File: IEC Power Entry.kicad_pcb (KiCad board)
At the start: 2 copper layers, 66 x 70.3 mm, 13 parts, among them J1 Primary, P3 DD21.0121.1111

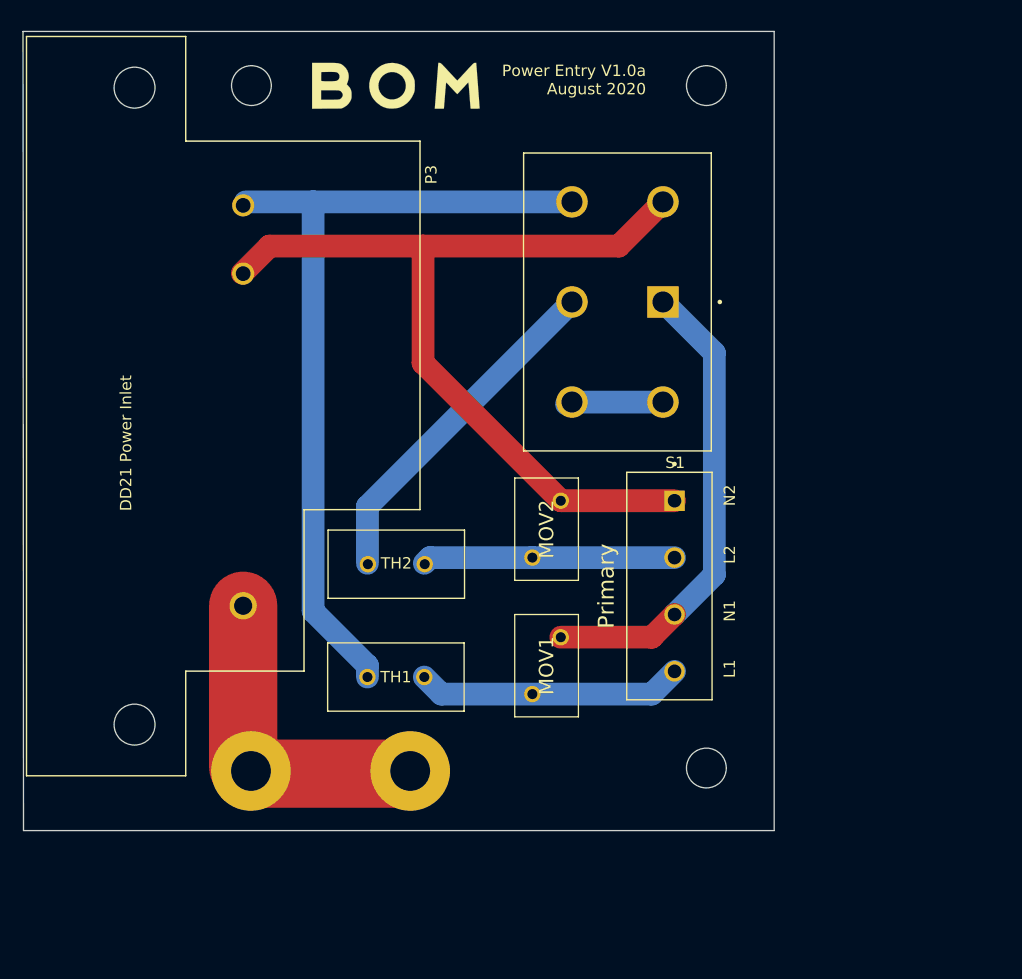
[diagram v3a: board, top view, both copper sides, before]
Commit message: feat: more track layout tweaking
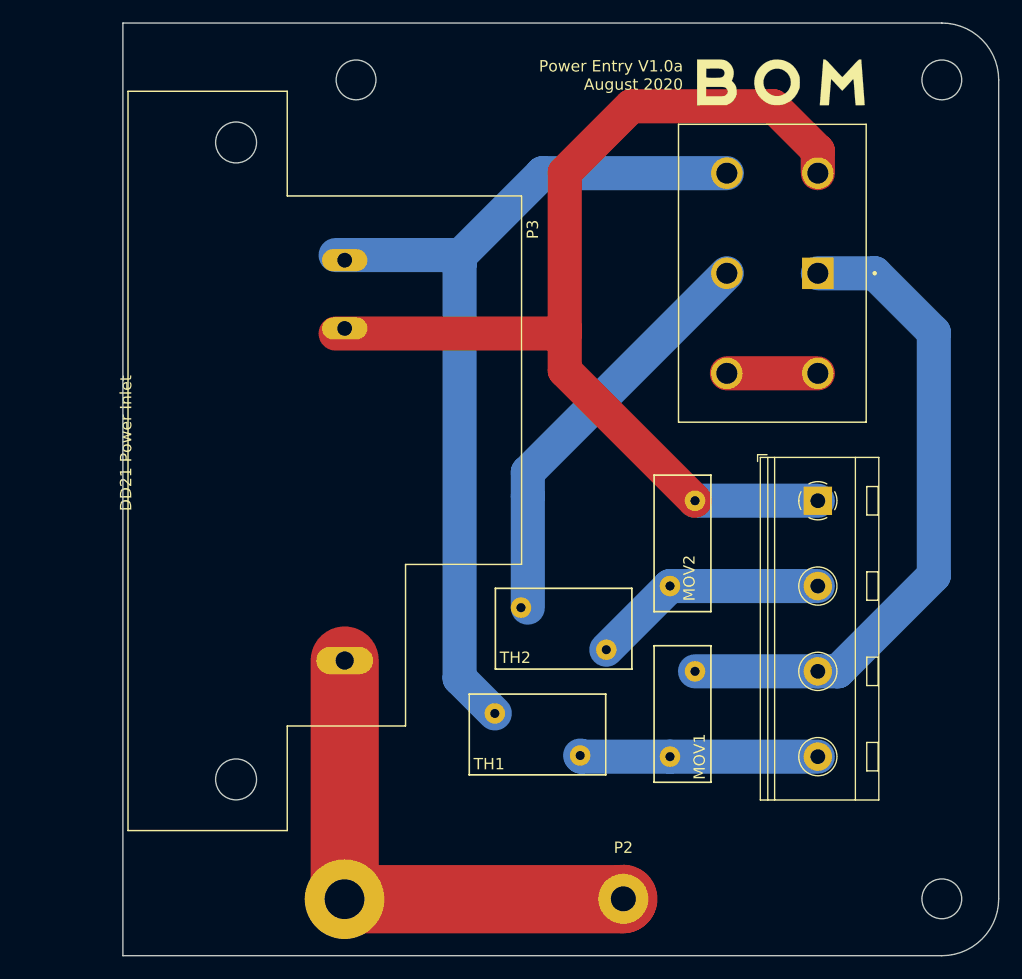
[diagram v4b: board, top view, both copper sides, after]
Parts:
- removed the REF** at (129.3, 127.8)
- removed the REF** at (143.3, 127.8)
- removed the REF** at (169.3, 67.5)
- removed the REF** at (169.3, 127.5)
- added P1: MountingHole_Pad, MountingHole:MountingHole_3.5mm_Pad, F.Cu at (137.5, 139.0)
- added P2: Chassis Ground, MountingHole:MountingHole_2.2mm_M2_Pad, F.Cu at (162.0, 139.0)
- added REF**: MountingHole_3.5mm, MountingHole:MountingHole_3.5mm, F.Cu at (190.0, 67.0)
- added REF**: MountingHole_3.5mm, MountingHole:MountingHole_3.5mm, F.Cu at (190.0, 139.0)
- J1: value Primary -> Transformer Primary; footprint TerminalBlock_TE-Connectivity:TerminalBlock_TE_1776266-4_1x4_P5mm_Horizonatal -> TerminalBlock_TE-Connectivity:TerminalBlock_TE-1546062-4_1x04_P7.50mm_Horizontal
- MOV1, MOV2: footprint Base on Mars Additions:V150LA2PX2855 -> Varistor:RV_Disc_D12mm_W5mm_P7.5mm
- TH1, TH2: footprint Base on Mars Additions:Thermistor_D8.5mm_W6mm_P5MM -> Varistor:RV_Disc_D12mm_W7.1mm_P7.5mm
- moved G*** 33.9 mm to (175.8, 67.2)
- moved TH1 16.7 mm to (158.2, 126.4)
- moved S1 13.9 mm to (175.1, 84.0)
- moved MOV1 13.3 mm to (166.1, 126.5)
- moved TH2 12.9 mm to (153.0, 113.4)
- moved J1 12.6 mm to (179.1, 104.0)
- moved MOV2 12.4 mm to (166.1, 111.5)
- moved P3 10.1 mm to (128.0, 100.5)
- moved REF** 9.21 mm to (138.5, 67.0)
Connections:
- P3 pad PE: Net-(P1-Pad1) -> Earth_Protective
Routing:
- net Earth_Protective: track 0.00 -> 45.5 mm
- net Net-(P1-Pad1): track 28.6 -> 0.00 mm
- net Net-(J1-Pad3): track 41.6 -> 58.2 mm
- net Net-(J1-Pad1): track 77.0 -> 92.8 mm
- net Net-(P3-PadL): track 72.5 -> 79.3 mm
- net Net-(S1-Pad2): track 30.4 -> 36.6 mm
- net Net-(J1-Pad4): track 23.4 -> 20.9 mm
- net Net-(J1-Pad2): track 22.2 -> 20.9 mm
- net Net-(S1-Pad1B): track 8.55 -> 8.00 mm
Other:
- board size 66 x 70.3 mm -> 77 x 82 mm
- net class Default: clearance 1.5 -> 3; trace_width 3 -> 2
- rule trace_clearance: 1.5 -> 3
- board text removed: "L1"
- board text removed: "L2"
- board text removed: "N1"
- board text removed: "N2"

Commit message: feat: add warning marks + silkscreen alignment
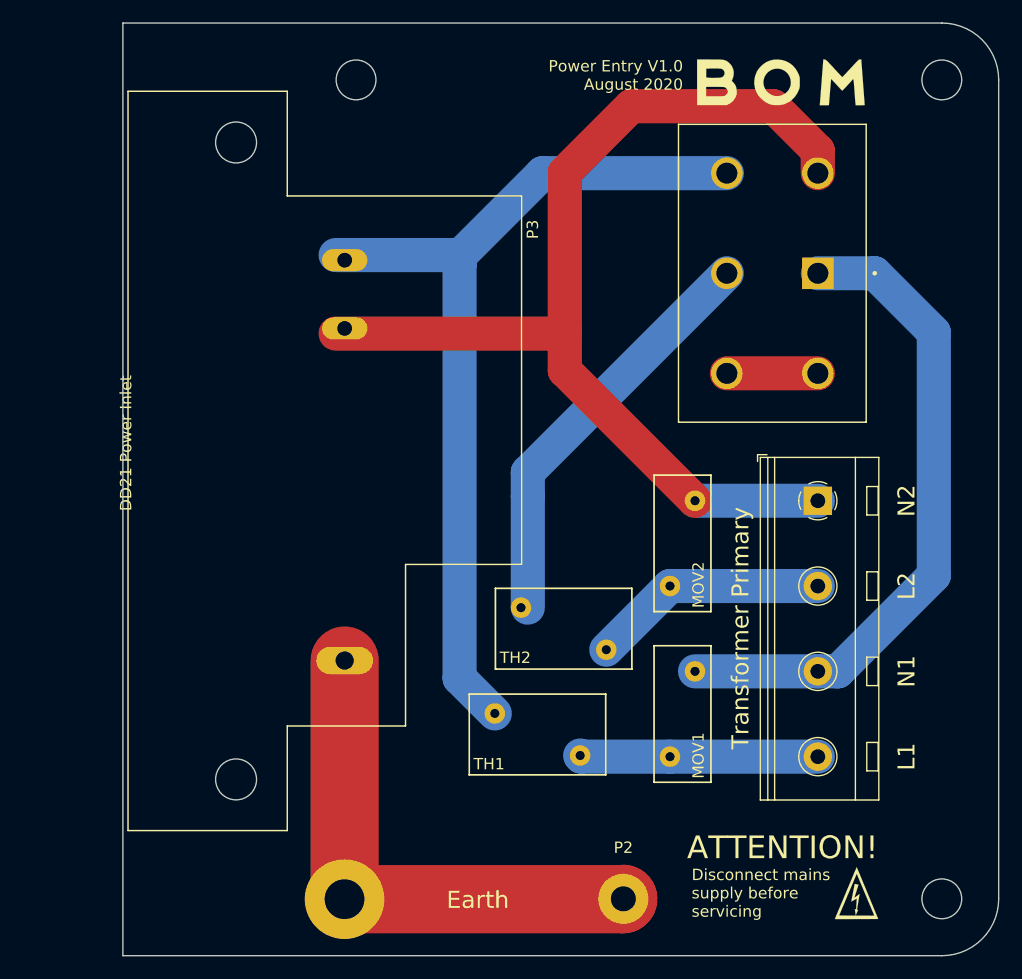
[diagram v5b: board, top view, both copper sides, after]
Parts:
- added G***: LOGO, TerminalBlock_RND:high_voltage_tiny, F.Cu at (182.5, 138.5)
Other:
- board text added: "ATTENTION!"
- board text added: "Disconnect mains supply before servicing"
- board text added: "Earth"
- board text added: "Power Entry V1.0 August 2020"
- board text removed: "Power Entry V1.0a August 2020"

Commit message: fix: adjust hole spacing for 70x50mm
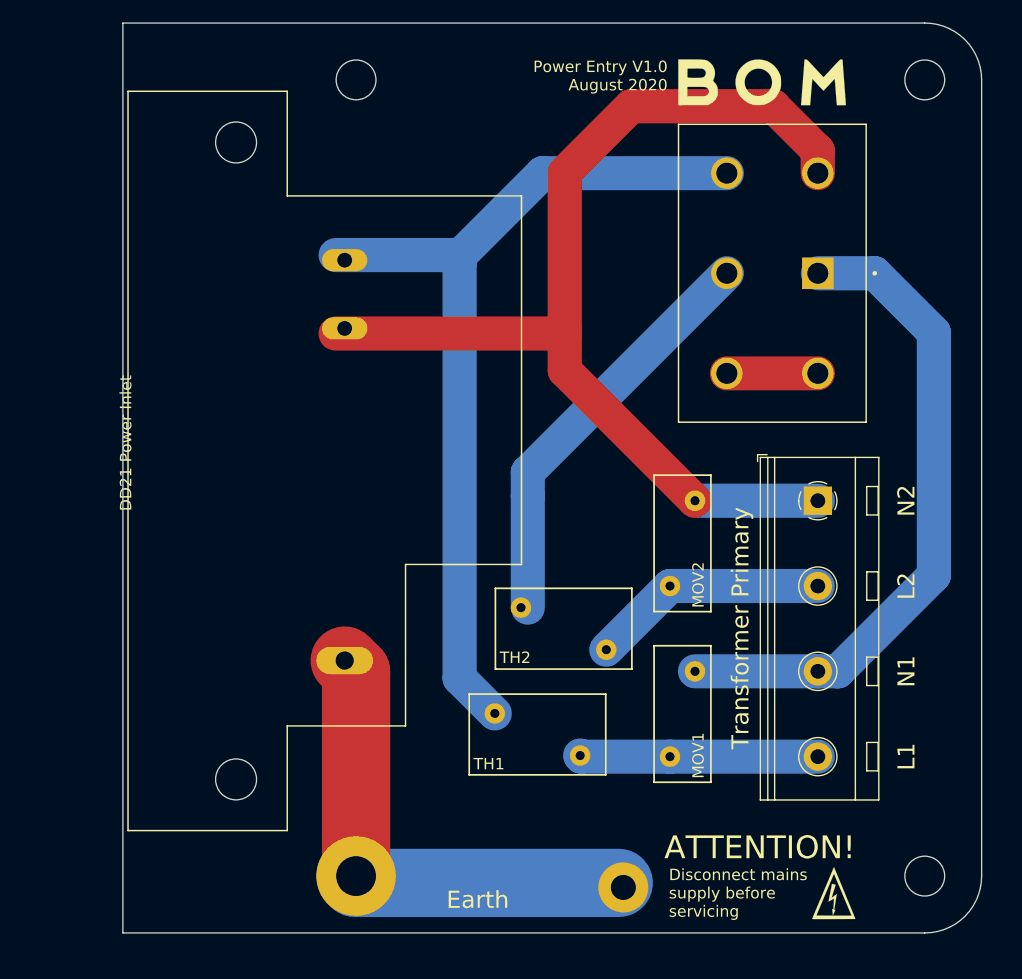
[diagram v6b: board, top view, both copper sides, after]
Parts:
- moved REF** 2.50 mm to (188.5, 137.0)
- moved P1 2.27 mm to (138.5, 137.0)
- moved G*** 2.00 mm to (180.5, 138.5)
- moved G*** 1.65 mm to (174.2, 67.2)
- moved REF** 1.50 mm to (188.5, 67.0)
- moved P2 1.00 mm to (162.0, 138.0)
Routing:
- net Earth_Protective: track 45.5 -> 42.6 mm
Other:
- board size 77 x 82 mm -> 75.5 x 80 mm
- net class Default: clearance 3 -> 0
- rule trace_clearance: 3 -> 0

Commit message: fix: tweak edge of board so that power module is flush
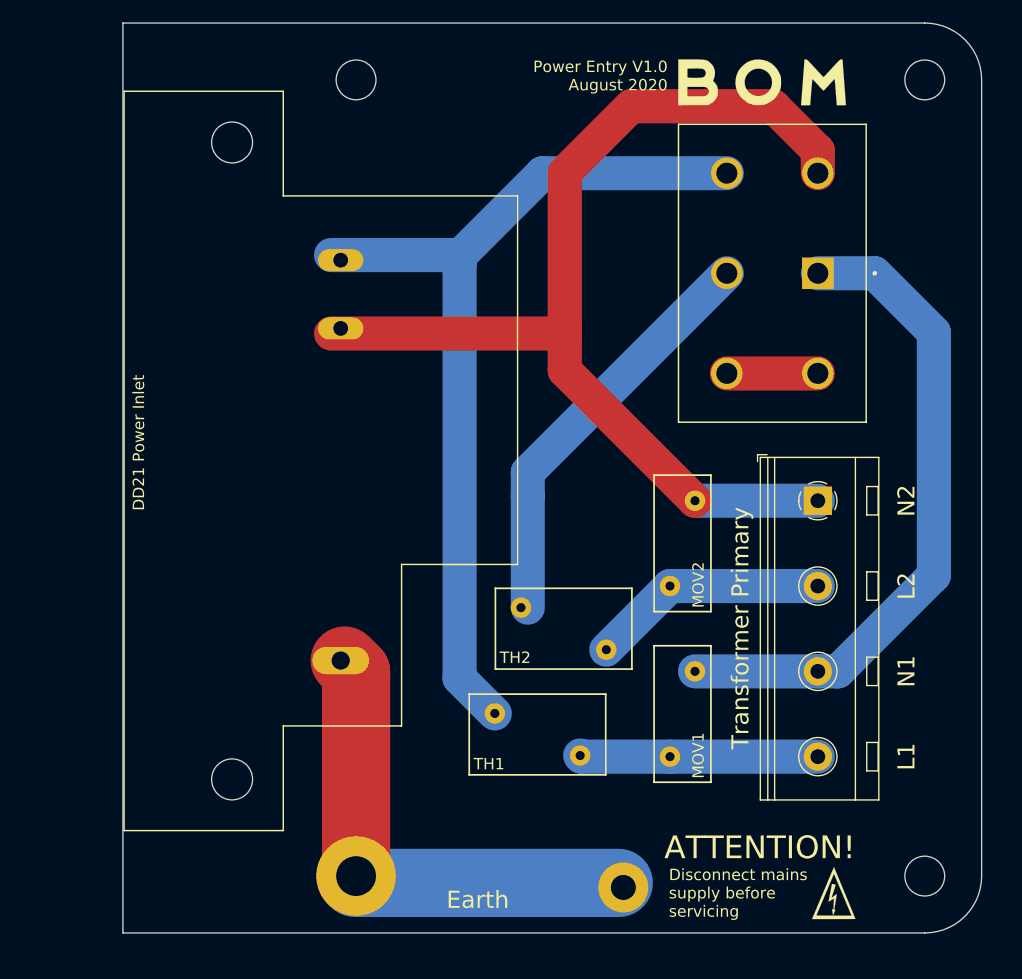
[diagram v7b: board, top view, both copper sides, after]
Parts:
- moved P3 0.35 mm to (127.6, 100.5)
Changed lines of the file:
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@@
   )
   (module "Base on Mars Additions:SCHURTER-DD21.0121.1111" (layer F.Cu)
-    (at 127.95 100.5 270)
+    (at 127.6 100.5 270)
     (descr "Schurter IEC Appliance Inlet C14 with Line Switch 2-pole, Fuseholder 1- or 2-pole, for PCB mounting,")
     (tags C14)
@@
   (gr_line (start 118 142) (end 118 62) (layer Edge.Cuts) (width 0.05))
   (gr_line (start 188.5 142) (end 118 142) (layer Edge.Cuts) (width 0.05))
-  (gr_text "DD21 Power Inlet" (at 118.2738 98.9331 90) (layer F.SilkS)
+  (gr_text "DD21 Power Inlet" (at 119.4 98.9 90) (layer F.SilkS)
     (effects (font (size 1 1) (thickness 0.15)))
   )
@@
   (segment (start 179.1 73.237779) (end 175.17472 69.312499) (width 3) (layer F.Cu) (net 4))
   (segment (start 179.1 75.2) (end 179.1 73.237779) (width 3) (layer F.Cu) (net 4))
-  (segment (start 136.7 89.3) (end 156.85 89.3) (width 3) (layer F.Cu) (net 4))
+  (segment (start 136.3 89.3) (end 156.85 89.3) (width 3) (layer F.Cu) (net 4))
   (segment (start 171.1 92.8) (end 179.1 92.8) (width 3) (layer F.Cu) (net 5))
   (segment (start 153.600009 103.599991) (end 153.600009 113.4) (width 3) (layer B.Cu) (net 6))
@@
   (segment (start 154.9 75.2) (end 147.25 82.85) (width 3) (layer B.Cu) (net 7))
   (segment (start 171.1 75.2) (end 154.9 75.2) (width 3) (layer B.Cu) (net 7))
-  (segment (start 136.7 82.4) (end 147.75 82.4) (width 3) (layer B.Cu) (net 7))
+  (segment (start 136.3 82.4) (end 147.75 82.4) (width 3) (layer B.Cu) (net 7))
+  (segment (start 138.4 137.6) (end 161.6 137.6) (width 6) (layer B.Cu) (net 8))
+  (segment (start 138.5 137) (end 138.5 119.05) (width 6) (layer F.Cu) (net 8))
   (segment (start 138.5 119.05) (end 137.5 118.05) (width 6) (layer F.Cu) (net 8))
-  (segment (start 138.5 137) (end 138.5 119.05) (width 6) (layer F.Cu) (net 8))
-  (segment (start 138.4 137.6) (end 161.6 137.6) (width 6) (layer B.Cu) (net 8))
 )

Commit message: chore: reapply clearance settings for board
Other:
- net class Default: clearance 0 -> 3
- rule trace_clearance: 0 -> 3
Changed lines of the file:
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@@
     (user_trace_width 5)
     (user_trace_width 6)
-    (trace_clearance 0)
+    (trace_clearance 3)
     (zone_clearance 0.508)
     (zone_45_only no)
@@
   (net 8 Earth_Protective)
   (net_class Default "This is the default net class."
-    (clearance 0)
+    (clearance 3)
     (trace_width 2)
     (via_dia 0.8)
@@
     (descr "Mounting Hole 2.2mm, M2")
     (tags "mounting hole 2.2mm m2")
+    (clearance 6)
     (attr virtual)
     (fp_text reference P2 (at 0 -4.5) (layer F.SilkS) hide
@@
     (descr "Mounting Hole 3.5mm")
     (tags "mounting hole 3.5mm")
+    (clearance 6)
     (attr virtual)
     (fp_text reference P1 (at 0 -4.5) (layer F.SilkS) hide
